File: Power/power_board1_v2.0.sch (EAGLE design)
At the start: 58 parts, among them J0_PLOAD_CONN 172648-0102, J1_B3_CONN 105313-1102, J2_LORA_CONN 105313-1102, J3_SPOT_CONN 105313-1102, J4_SSSBOARD_CONN 172648-0102, Q1 FQD11P06TM

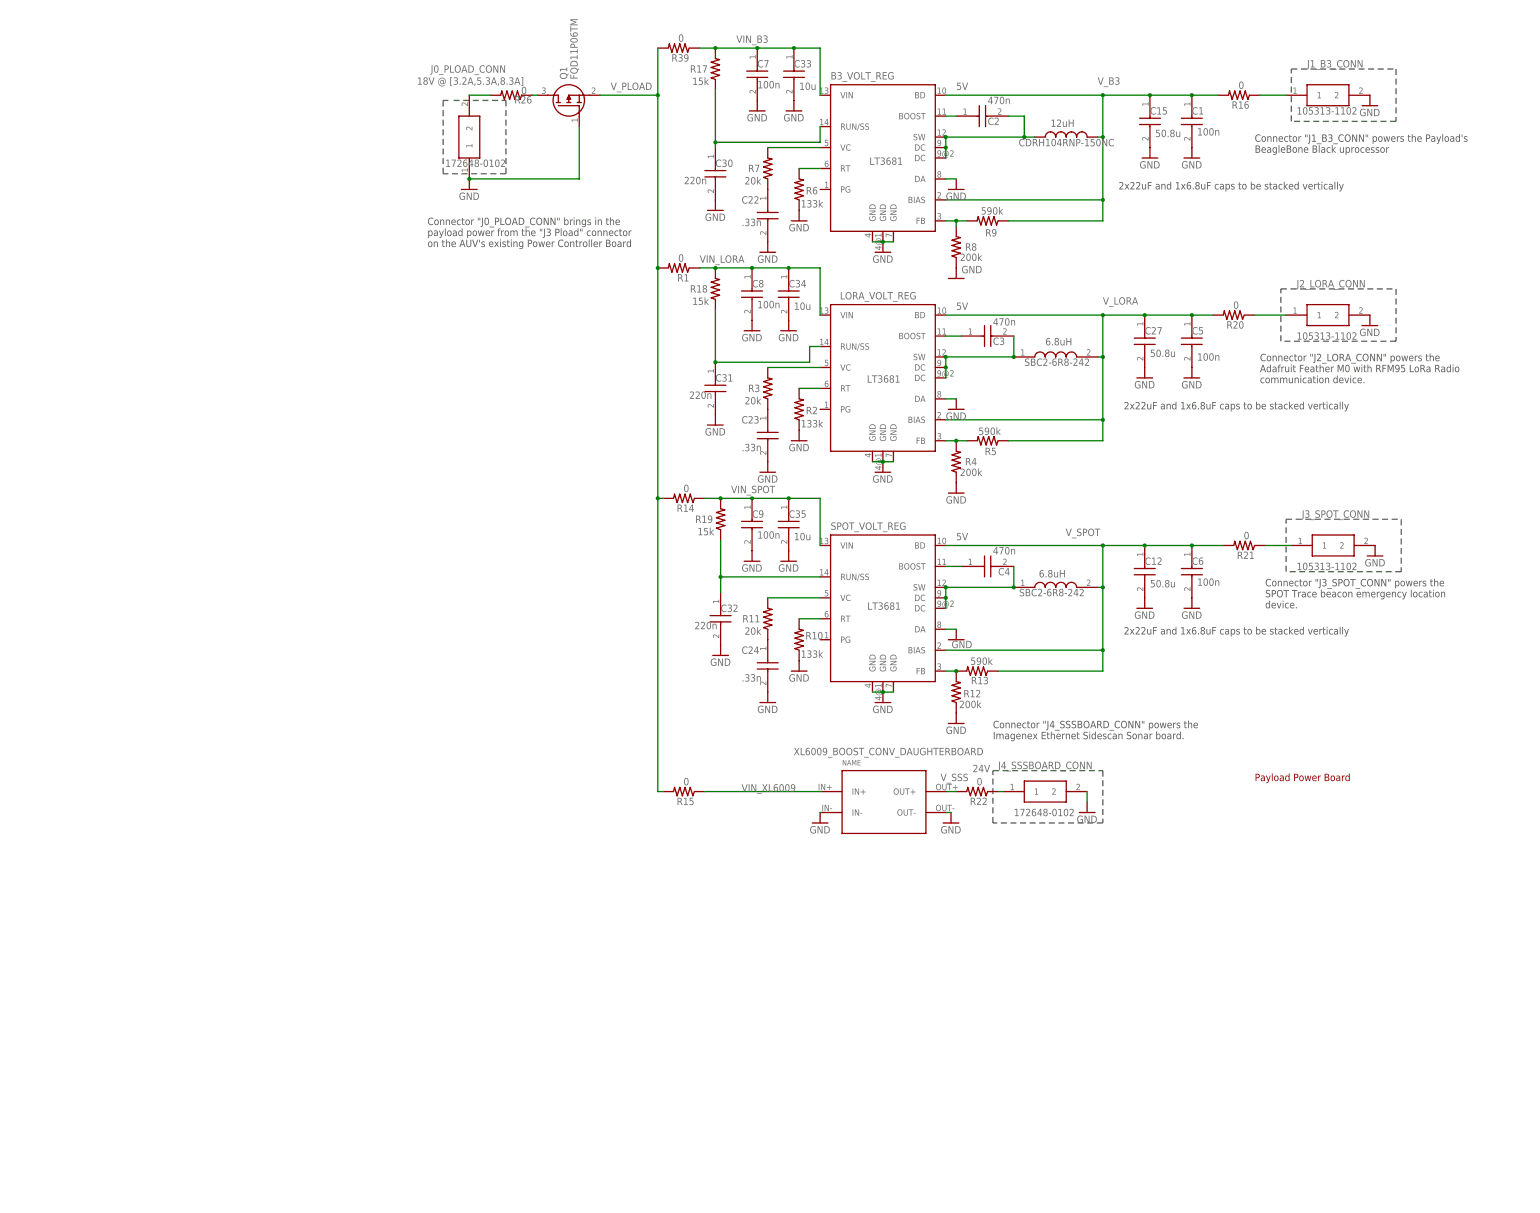
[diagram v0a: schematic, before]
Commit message: Redesigned layout to fit in AUV. Changed 18V and 24V to mini and micro (also vertical), tucked connectors into board, all wrapped up
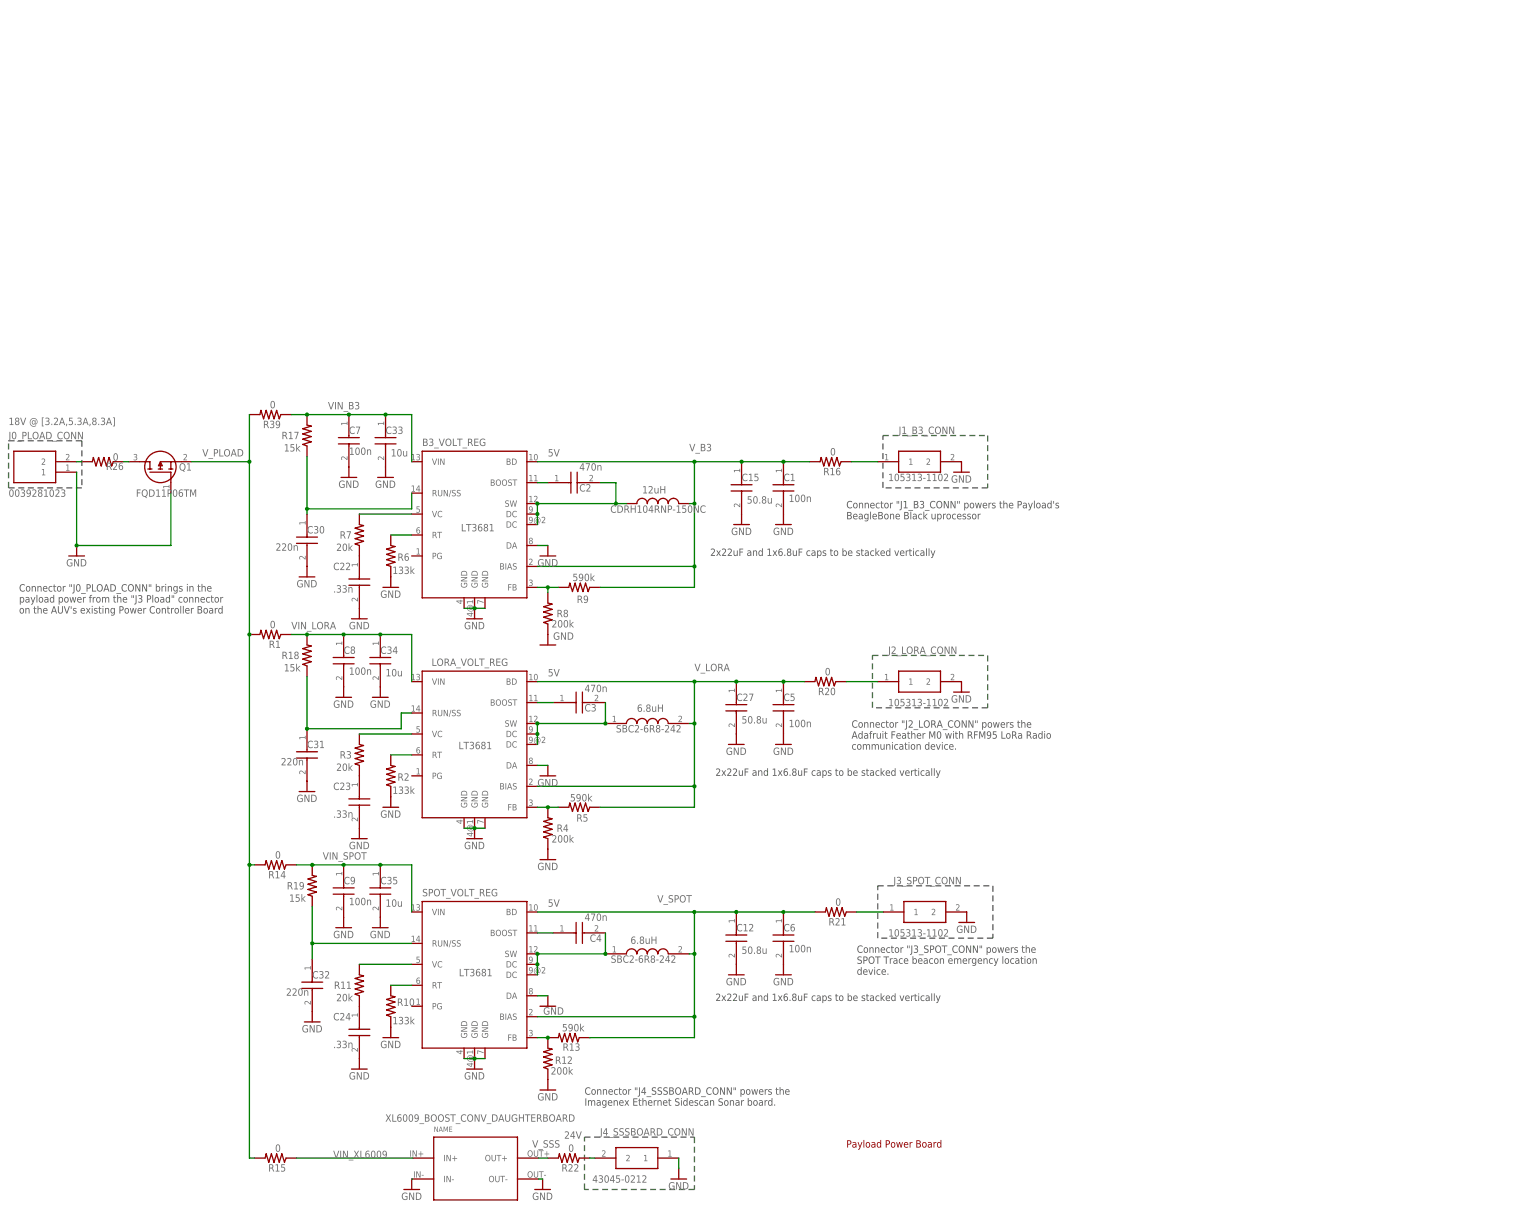
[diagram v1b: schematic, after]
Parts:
- J0_PLOAD_CONN: value 172648-0102 -> 0039281023; device 172648-0102:172648-0102 -> 0039281023:0039281023
- J4_SSSBOARD_CONN: value 172648-0102 -> 43045-0212; device 172648-0102:172648-0102 -> 43045-0212:43045-0212
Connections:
- net GND: now also J4_SSSBOARD_CONN.1; no longer J4_SSSBOARD_CONN.2
- net V_SSS1: now also J4_SSSBOARD_CONN.2; no longer J4_SSSBOARD_CONN.1
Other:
- moved on the sheet: B3_VOLT_REG, C1, C12, C15, C2, C22, C23, C24, C27, C3, C30, C31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

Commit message: Forgot to add names to components (helpful for assembly)
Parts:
- XL6009_BOOST_CONV_DAUGHTERBOARD: value CP8-ADJ -> XL6009
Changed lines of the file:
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@@
 <part name="GND21" library="supply1" library_urn="urn:adsk.eagle:library:371" deviceset="GND" device=""/>
 <part name="GND22" library="supply1" library_urn="urn:adsk.eagle:library:371" deviceset="GND" device=""/>
-<part name="XL6009_BOOST_CONV_DAUGHTERBOARD" library="userlib" deviceset="CP8-ADJ" device=""/>
+<part name="XL6009_BOOST_CONV_DAUGHTERBOARD" library="userlib" deviceset="CP8-ADJ" device="" value="XL6009"/>
 <part name="GND26" library="supply1" library_urn="urn:adsk.eagle:library:371" deviceset="GND" device=""/>
 <part name="GND27" library="supply1" library_urn="urn:adsk.eagle:library:371" deviceset="GND" device=""/>

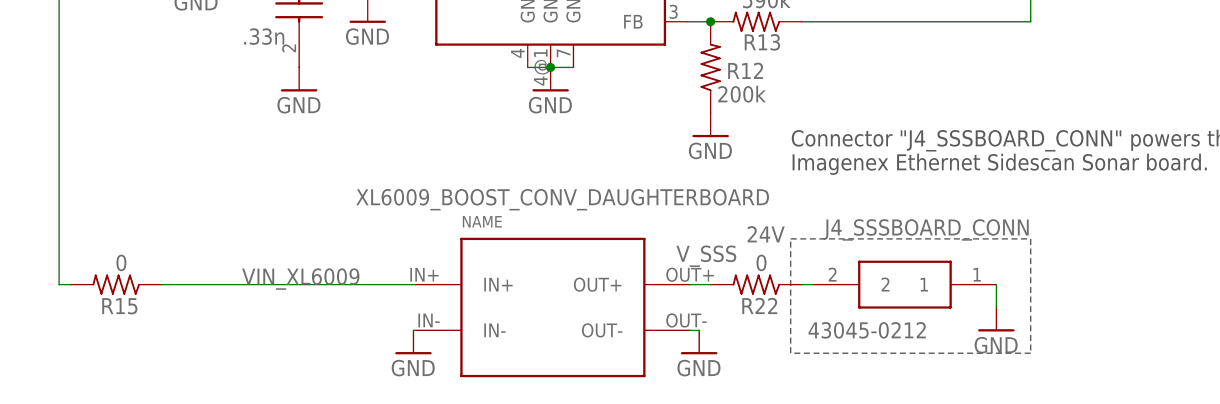
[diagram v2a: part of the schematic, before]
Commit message: Boards being made at OSHPark were wrt these files
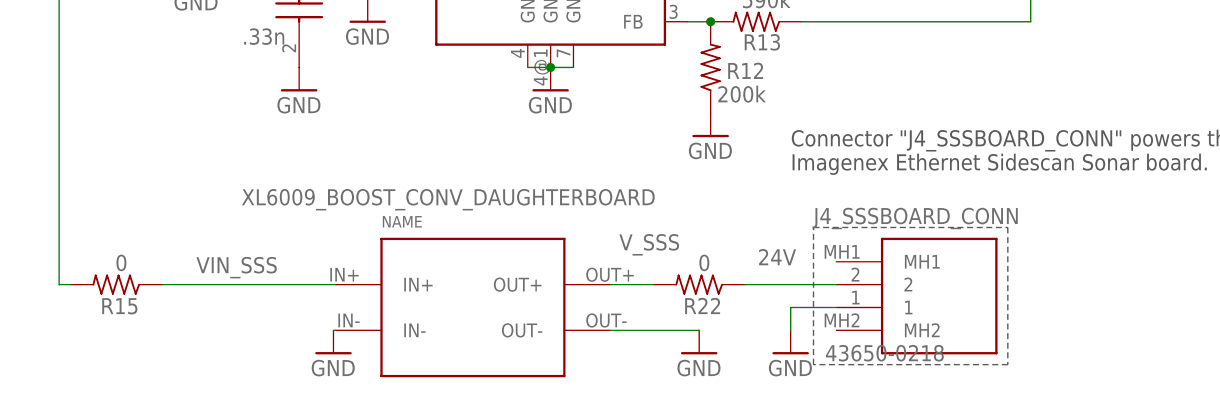
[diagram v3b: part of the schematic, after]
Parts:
- J4_SSSBOARD_CONN: value 43045-0212 -> 43650-0218; device 43045-0212:43045-0212 -> 43650-0218:43650-0218
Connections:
- net VIN_XL6009 renamed VIN_SSS
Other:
- moved on the sheet: R22
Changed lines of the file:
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@@
 <part name="Q1" library="FQD11P06TM" deviceset="FQD11P06TM" device=""/>
 <part name="J0_PLOAD_CONN" library="0039281023" deviceset="0039281023" device=""/>
-<part name="J4_SSSBOARD_CONN" library="43045-0212" deviceset="43045-0212" device=""/>
+<part name="J4_SSSBOARD_CONN" library="43650-0218" deviceset="43650-0218" device=""/>
 </parts>
 <sheets>
 <sheet>
 <plain>
-<text x="96.45" y="34.22" size="1.778" layer="95">XL6009_BOOST_CONV_DAUGHTERBOARD</text>
-<text x="139.84" y="30.09" size="1.778" layer="95">24V</text>
+<text x="83.75" y="34.22" size="1.778" layer="95">XL6009_BOOST_CONV_DAUGHTERBOARD</text>
+<text x="141.11" y="27.55" size="1.778" layer="95">24V</text>
 <text x="155.92" y="77.35" size="1.778" layer="96">6.8uH</text>
 <text x="157.49" y="133.63" size="1.778" layer="96">6.8uH</text>
@@
 <wire x1="243.84" y1="78.74" x2="215.9" y2="78.74" width="0.1524" layer="97" style="shortdash"/>
 <wire x1="215.9" y1="78.74" x2="215.9" y2="91.44" width="0.1524" layer="97" style="shortdash"/>
-<wire x1="144.78" y1="30.48" x2="171.45" y2="30.48" width="0.1524" layer="97" style="shortdash"/>
-<wire x1="171.45" y1="30.48" x2="171.45" y2="17.78" width="0.1524" layer="97" style="shortdash"/>
-<wire x1="171.45" y1="17.78" x2="144.78" y2="17.78" width="0.1524" layer="97" style="shortdash"/>
-<wire x1="144.78" y1="17.78" x2="144.78" y2="30.48" width="0.1524" layer="97" style="shortdash"/>
+<wire x1="147.32" y1="31.75" x2="168.91" y2="31.75" width="0.1524" layer="97" style="shortdash"/>
+<wire x1="168.91" y1="31.75" x2="168.91" y2="16.51" width="0.1524" layer="97" style="shortdash"/>
+<wire x1="168.91" y1="16.51" x2="147.32" y2="16.51" width="0.1524" layer="97" style="shortdash"/>
+<wire x1="147.32" y1="16.51" x2="147.32" y2="31.75" width="0.1524" layer="97" style="shortdash"/>
 <text x="208.28" y="180.34" size="1.778" layer="97">Connector "J1_B3_CONN" powers the Payload's
 BeagleBone Black uprocessor</text>
@@
 <attribute name="VALUE" x="95.25" y="52.07" size="1.778" layer="96"/>
 </instance>
-<instance part="XL6009_BOOST_CONV_DAUGHTERBOARD" gate="G$1" x="118.11" y="22.86" smashed="yes"/>
+<instance part="XL6009_BOOST_CONV_DAUGHTERBOARD" gate="G$1" x="109.22" y="22.86" smashed="yes"/>
 <instance part="GND26" gate="1" x="134.62" y="17.78" smashed="yes">
 <attribute name="VALUE" x="132.08" y="15.24" size="1.778" layer="96"/>
 </instance>
-<instance part="GND27" gate="1" x="102.87" y="17.78" smashed="yes">
-<attribute name="VALUE" x="100.33" y="15.24" size="1.778" layer="96"/>
+<instance part="GND27" gate="1" x="93.98" y="17.78" smashed="yes">
+<attribute name="VALUE" x="91.44" y="15.24" size="1.778" layer="96"/>
 </instance>
 <instance part="R17" gate="G$1" x="77.47" y="200.66" smashed="yes" rot="R90">
@@
 <attribute name="VALUE" x="233.68" y="189.23" size="1.778" layer="96"/>
 </instance>
-<instance part="GND23" gate="1" x="167.64" y="20.32" smashed="yes">
-<attribute name="VALUE" x="165.1" y="17.78" size="1.778" layer="96"/>
+<instance part="GND23" gate="1" x="144.78" y="17.78" smashed="yes">
+<attribute name="VALUE" x="142.24" y="15.24" size="1.778" layer="96"/>
 </instance>
 <instance part="GND24" gate="1" x="237.49" y="82.55" smashed="yes">
@@
 <attribute name="DESC" x="205.74" y="85.09" size="1.778" layer="96" rot="R180" display="off"/>
 </instance>
-<instance part="R22" gate="G$1" x="140.97" y="25.4" smashed="yes" rot="R180">
-<attribute name="NAME" x="143.51" y="23.9014" size="1.778" layer="95" rot="R180"/>
-<attribute name="VALUE" x="142.24" y="28.702" size="1.778" layer="96" rot="R180"/>
-<attribute name="MFR" x="140.97" y="25.4" size="1.778" layer="96" rot="R180" display="off"/>
-<attribute name="MPN" x="140.97" y="25.4" size="1.778" layer="96" rot="R180" display="off"/>
-<attribute name="DESC" x="140.97" y="25.4" size="1.778" layer="96" rot="R180" display="off"/>
+<instance part="R22" gate="G$1" x="134.62" y="25.4" smashed="yes" rot="R180">
+<attribute name="NAME" x="137.16" y="23.9014" size="1.778" layer="95" rot="R180"/>
+<attribute name="VALUE" x="135.89" y="28.702" size="1.778" layer="96" rot="R180"/>
+<attribute name="MFR" x="134.62" y="25.4" size="1.778" layer="96" rot="R180" display="off"/>
+<attribute name="MPN" x="134.62" y="25.4" size="1.778" layer="96" rot="R180" display="off"/>
+<attribute name="DESC" x="134.62" y="25.4" size="1.778" layer="96" rot="R180" display="off"/>
 </instance>
 <instance part="R26" gate="G$1" x="27.94" y="194.31" smashed="yes" rot="R180">
@@
 <attribute name="VALUE" x="5.08" y="186.69" size="1.778" layer="96" align="center-left"/>
 </instance>
-<instance part="J4_SSSBOARD_CONN" gate="G$1" x="167.64" y="25.4" smashed="yes" rot="R180">
-<attribute name="NAME" x="171.45" y="31.75" size="1.778" layer="95" rot="R180" align="center-left"/>
-<attribute name="VALUE" x="160.02" y="20.32" size="1.778" layer="96" rot="R180" align="center-left"/>
+<instance part="J4_SSSBOARD_CONN" gate="G$1" x="149.86" y="27.94" smashed="yes">
+<attribute name="NAME" x="147.32" y="33.02" size="1.778" layer="95" align="center-left"/>
+<attribute name="VALUE" x="148.59" y="17.78" size="1.778" layer="96" align="center-left"/>
 </instance>
 </instances>
@@
 <pinref part="XL6009_BOOST_CONV_DAUGHTERBOARD" gate="G$1" pin="OUT-"/>
 <pinref part="GND26" gate="1" pin="GND"/>
-<wire x1="133.604" y1="20.32" x2="134.62" y2="20.32" width="0.1524" layer="91"/>
+<wire x1="124.714" y1="20.32" x2="134.62" y2="20.32" width="0.1524" layer="91"/>
 </segment>
 <segment>
 <pinref part="XL6009_BOOST_CONV_DAUGHTERBOARD" gate="G$1" pin="IN-"/>
 <pinref part="GND27" gate="1" pin="GND"/>
-<wire x1="103.124" y1="20.32" x2="102.87" y2="20.32" width="0.1524" layer="91"/>
-</segment>
-<segment>
-<wire x1="167.64" y1="22.86" x2="167.64" y2="25.4" width="0.1524" layer="91"/>
-<pinref part="GND23" gate="1" pin="GND"/>
-<pinref part="J4_SSSBOARD_CONN" gate="G$1" pin="1"/>
+<wire x1="94.234" y1="20.32" x2="93.98" y2="20.32" width="0.1524" layer="91"/>
 </segment>
 <segment>
@@
 <pinref part="C7" gate="G$1" pin="2"/>
 <pinref part="GND31" gate="1" pin="GND"/>
+</segment>
+<segment>
+<pinref part="J4_SSSBOARD_CONN" gate="G$1" pin="1"/>
+<pinref part="GND23" gate="1" pin="GND"/>
+<wire x1="149.86" y1="22.86" x2="144.78" y2="22.86" width="0.1524" layer="91"/>
+<wire x1="144.78" y1="22.86" x2="144.78" y2="20.32" width="0.1524" layer="91"/>
 </segment>
 </net>
@@
 </segment>
 </net>
-<net name="VIN_XL6009" class="0">
+<net name="VIN_SSS" class="0">
 <segment>
 <pinref part="R15" gate="G$1" pin="1"/>
 <pinref part="XL6009_BOOST_CONV_DAUGHTERBOARD" gate="G$1" pin="IN+"/>
-<wire x1="74.93" y1="25.4" x2="103.124" y2="25.4" width="0.1524" layer="91"/>
-<label x="83.82" y="25.4" size="1.778" layer="95"/>
+<wire x1="74.93" y1="25.4" x2="94.234" y2="25.4" width="0.1524" layer="91"/>
+<label x="78.74" y="26.67" size="1.778" layer="95"/>
 </segment>
 </net>
@@
 <pinref part="XL6009_BOOST_CONV_DAUGHTERBOARD" gate="G$1" pin="OUT+"/>
 <pinref part="R22" gate="G$1" pin="2"/>
-<wire x1="133.604" y1="25.4" x2="135.89" y2="25.4" width="0.1524" layer="91"/>
-<label x="132.08" y="27.94" size="1.778" layer="95"/>
+<wire x1="124.714" y1="25.4" x2="129.54" y2="25.4" width="0.1524" layer="91"/>
+<label x="125.73" y="29.21" size="1.778" layer="95"/>
 </segment>
 </net>
@@
 <segment>
 <pinref part="R22" gate="G$1" pin="1"/>
-<wire x1="147.32" y1="25.4" x2="146.05" y2="25.4" width="0.1524" layer="91"/>
+<wire x1="149.86" y1="25.4" x2="139.7" y2="25.4" width="0.1524" layer="91"/>
 <pinref part="J4_SSSBOARD_CONN" gate="G$1" pin="2"/>
 </segment>
